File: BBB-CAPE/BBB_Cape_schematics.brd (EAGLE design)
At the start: 160 x 176.5 mm, 94 parts, among them IC1 EEPROM-I2CSMD, SW2 219-02, U5 TPS60403

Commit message: Route all components in PCB in BBB_Cape_schematics.brd
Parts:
- removed C1: 0.1uF, logic-supply:C0402
- removed C11: 0.0015uF, rcl:C1206
- removed IC1: EEPROM-I2CSMD, logic-supply:SO08
- removed R1, R2, R3, R4, R5, R6: 5.6k, logic-supply:R0402
- removed R25: 4.99k, resistor:M1206
- removed S2, SW2: 219-02, switch-dil:CTS-219-02
- removed SJ10, SJ11, SJ12, SJ13, SJ2, SJ3, SJ4, SJ5, SJ6, SJ7, SJ8, SJ9: (no value), jumper:SJW
- removed TP1, TP2: TEST_POINT, logic-supply:TEST_POINT
- removed TP1_2.5V, TP_INA_VREF: TPB2,54, testpad:B2,54
- removed U$10: CDCS502, Components:SSOP-8
- removed U$13, U$9: OPA335, Components:SOT23-5
- removed U$16, U$18: PAD, Components:RECT_PAD
- removed U$19: ADS1252, Components:SOIC-8
- removed U$23: ATS16ASM-1, Components:CRYSTAL_SMD
- added JP1, JP2: (no value), jumper:JP3Q
- added JP3: (no value), jumper:JP2
- added JP4, JP5: (no value), jumper:JP2Q
- added LH, LH_INDEX: PAD, Components:RECT_PAD
- added U10: CDCS502, Components:SSOP-8
- added U13, U9: OPA335, Components:SOT23-5
- added U19: ADS1252, Components:SOIC-8
- added U23: ATS16ASM-1, Components:CRYSTAL_SMD
- moved TP_5V 283.6 mm to (72.0, 16.6)
- moved TP5 250.2 mm to (69.0, 46.5)
- moved TP_ECG_INA 250.1 mm to (73.4, 9.44)
- moved TP2_MIN5V 243.6 mm to (94.7, 61.6)
- moved TP4 235.5 mm to (57.0, 43.5)
- moved TP3 235.4 mm to (57.0, 49.2)
- moved TP_3.3V 221.9 mm to (45.4, 71.1)
- moved TP_ECG_LPF 220.4 mm to (77.8, 39.7)
- moved TP1_MIN5V 212.6 mm to (70.3, 67.2)
- moved TP2_2.5V 46.8 mm to (56.6, 34.5)
- moved R24 15.0 mm to (68.6, 34.0), turned to 180 degrees
- moved C10 12.7 mm to (77.5, 35.1), turned to 0 degrees
- moved R18 12.1 mm to (87.0, 26.4), turned to 270 degrees
- moved R17 11.4 mm to (68.6, 29.0), turned to 180 degrees
- moved R26 11.2 mm to (68.6, 23.9), turned to 180 degrees
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- renumbered U$11 to U11, U$12 to U12, U$14 to U14, U$17 to RH, U$21 to U21, U$22 to U22, U$24 to RH_INDEX, U$4 to U4
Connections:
- removed net N$13: IC1.1, R3.1, SW2.4
- removed net N$14: IC1.2, R2.1, SW2.3
- removed net N$15: IC1.3, R1.1
- removed net N$39: R26.2, SJ7.2
- removed net N$43: C20.1, SJ13.2
- removed net WP: IC1.7, R4.1, TP2.P$1
- net +5V/2: now also U13.P$3, U19.P$2, U19.P$8, U9.P$3; no longer U$13.P$3, U$19.P$2, U$19.P$8, U$9.P$3
- net 3.3V: now also JP5.2, JP5.4, U10.7; no longer C1.1, IC1.8, R1.2, R2.2, R3.2, R4.2, R5.2, R6.2, S2.1, S2.2, U$10.7
- net 5V: now also U13.P$5, U19.P$3, U9.P$5; no longer U$13.P$5, U$19.P$3, U$9.P$5
- net ADC_DOUT: now also U19.P$5; no longer U$19.P$5
- net ADC_SCLK: now also U19.P$6; no longer U$19.P$6
- net ECG_LPF: now also U13.P$1, U19.P$1; no longer C11.2, U$13.P$1, U$19.P$1
- net GND: now also JP3.2, U10.4, U10.5, U13.P$2, U19.P$7, U9.P$2; no longer C1.2, IC1.4, SJ8.1, SW2.1, SW2.2, TP1.P$1, U$10.4, U$10.5, U$13.P$2, U$19.P$7, U$9.P$2
- net I2C2_SCL: no longer IC1.6, R5.1
- net I2C2_SDA: no longer IC1.5, R6.1
- net N$10: now also JP3.3; no longer SJ8.2, SJ9.2
- net N$11: now also JP1.2, JP1.4, JP1.6, JP4.2, JP4.4; no longer SJ2.1, SJ3.1, SJ4.1, SJ5.1, SJ6.1, SJ7.1
- net N$12: now also U9.P$4; no longer U$9.P$4
- net N$18: now also JP2.2, JP2.4, JP2.6, U13.P$4; no longer R25.1, SJ10.1, SJ11.1, SJ12.1, SJ13.1, U$13.P$4
- net N$22: now also LH_INDEX.P$1; no longer U$18.P$1
- net N$24: now also LH.P$1; no longer U$16.P$1
- net N$26: no longer TP1_2.5V.TP
- net N$27: now also U10.1, U23.P$1; no longer U$10.1, U$23.P$1
- net N$28: now also U10.8, U23.P$2; no longer U$10.8, U$23.P$2
- net N$29: now also U10.6, U19.P$4; no longer U$10.6, U$19.P$4
- net N$30: now also JP5.3, U10.2; no longer S2.4, U$10.2
- net N$31: now also JP5.1, U10.3; no longer S2.3, U$10.3
- net N$33: now also JP4.3; no longer SJ2.2
- net N$34: now also JP4.1; no longer SJ3.2
- net N$35: now also JP3.1, U9.P$1; no longer SJ9.1, TP_INA_VREF.TP, U$9.P$1
- net N$36: now also JP1.5, R24.2; no longer R25.2, SJ4.2
- net N$37: now also JP1.3, R17.2; no longer R24.2, SJ5.2
- net N$38: now also JP1.1, R26.2; no longer R17.2, SJ6.2
- net N$40: now also C10.1, JP2.5; no longer C11.1, SJ10.2
- net N$41: now also C21.1, JP2.3; no longer C10.1, SJ11.2
- net N$42: now also C20.1, JP2.1; no longer C21.1, SJ12.2
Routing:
- net 5V: track 198.7 -> 298.7 mm
- net 3.3V: track 2.54 -> 66.3 mm, vias 0 -> 1
- net ECG_LPF: track 0.00 -> 51.0 mm
- net N$18: track 0.00 -> 46.9 mm
- net N$11: track 8.62 -> 43.6 mm
- net +5V/2: track 135.9 -> 168.3 mm, vias 1 -> 4
- net N$10: track 6.04 -> 35.5 mm
- net N$12: track 10.1 -> 28.7 mm
- net N$30: track 0.00 -> 15.7 mm
- net GND: track 25.0 -> 38.9 mm, vias 9 -> 41
- net ADC_DOUT: track 0.00 -> 12.7 mm
- net ADC_SCLK: track 0.00 -> 11.7 mm
- net N$29: track 0.00 -> 10.4 mm
- net N$31: track 0.00 -> 10.4 mm
- net N$38: track 0.00 -> 6.15 mm
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- added copper zone on layer 1, net GND

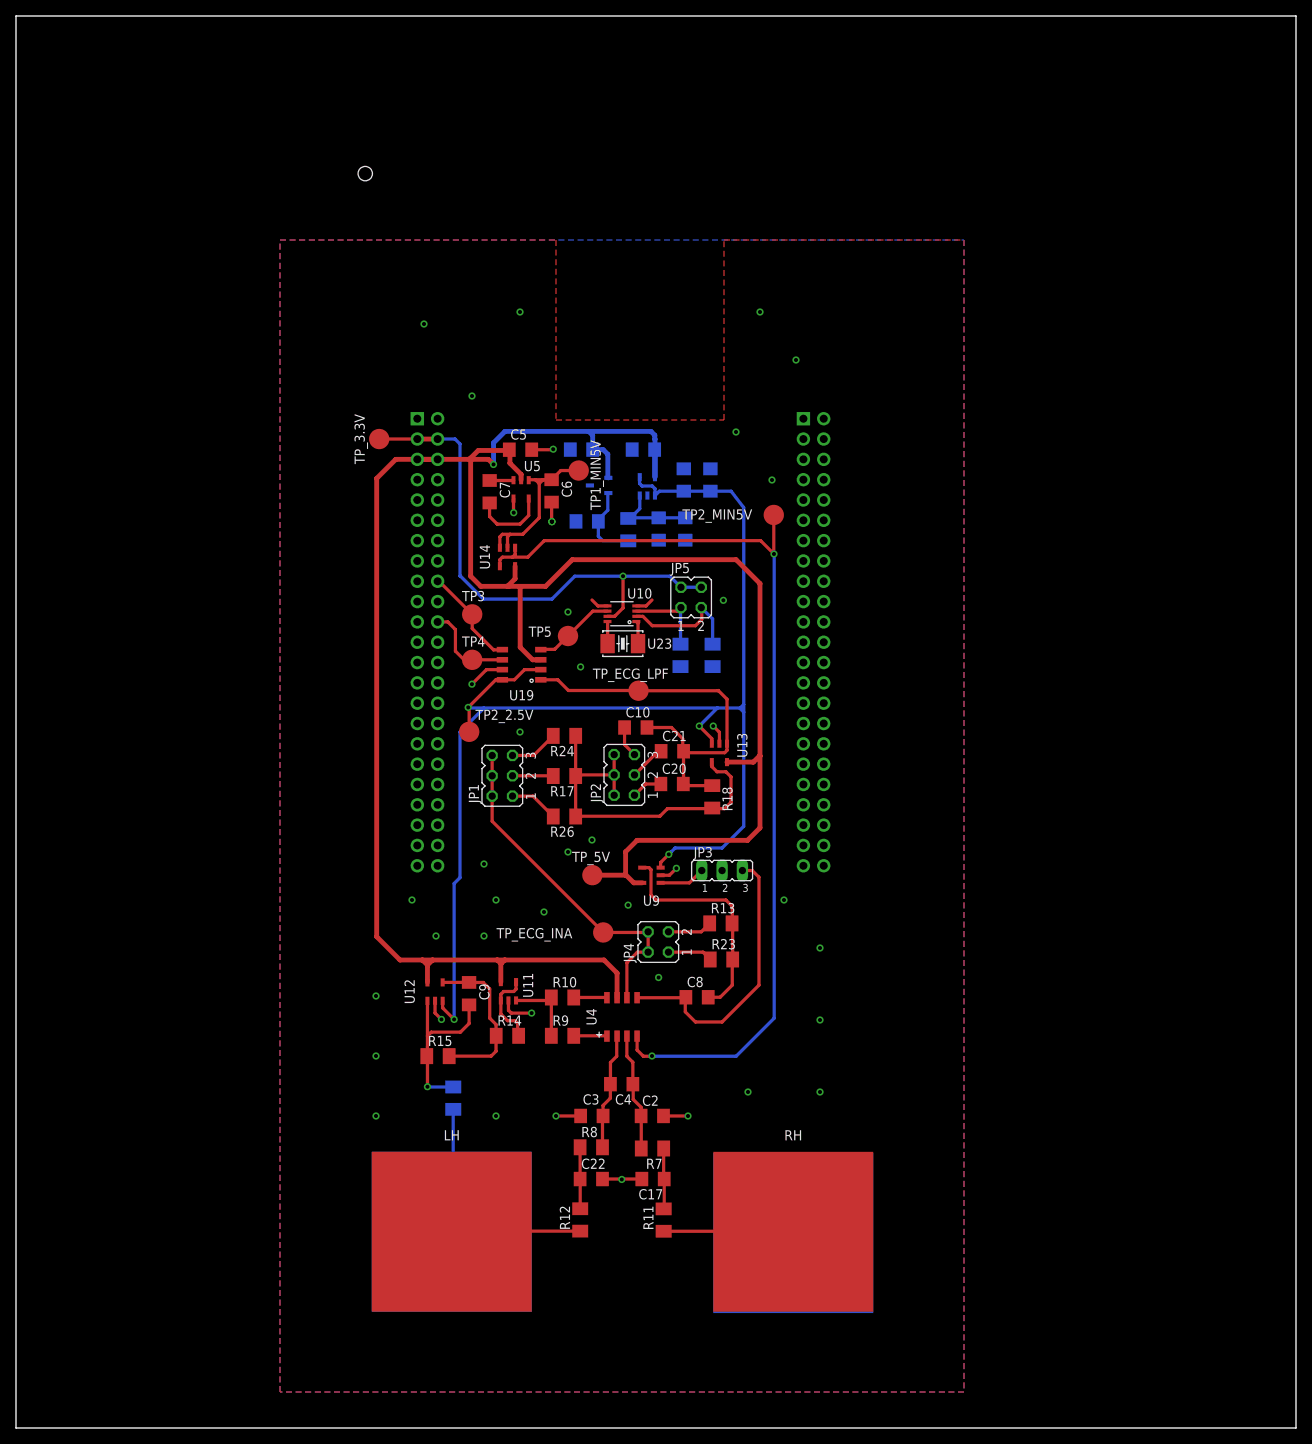
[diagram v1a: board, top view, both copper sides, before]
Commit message: Modify board boundary, Change orientation of Component names in Silk screen
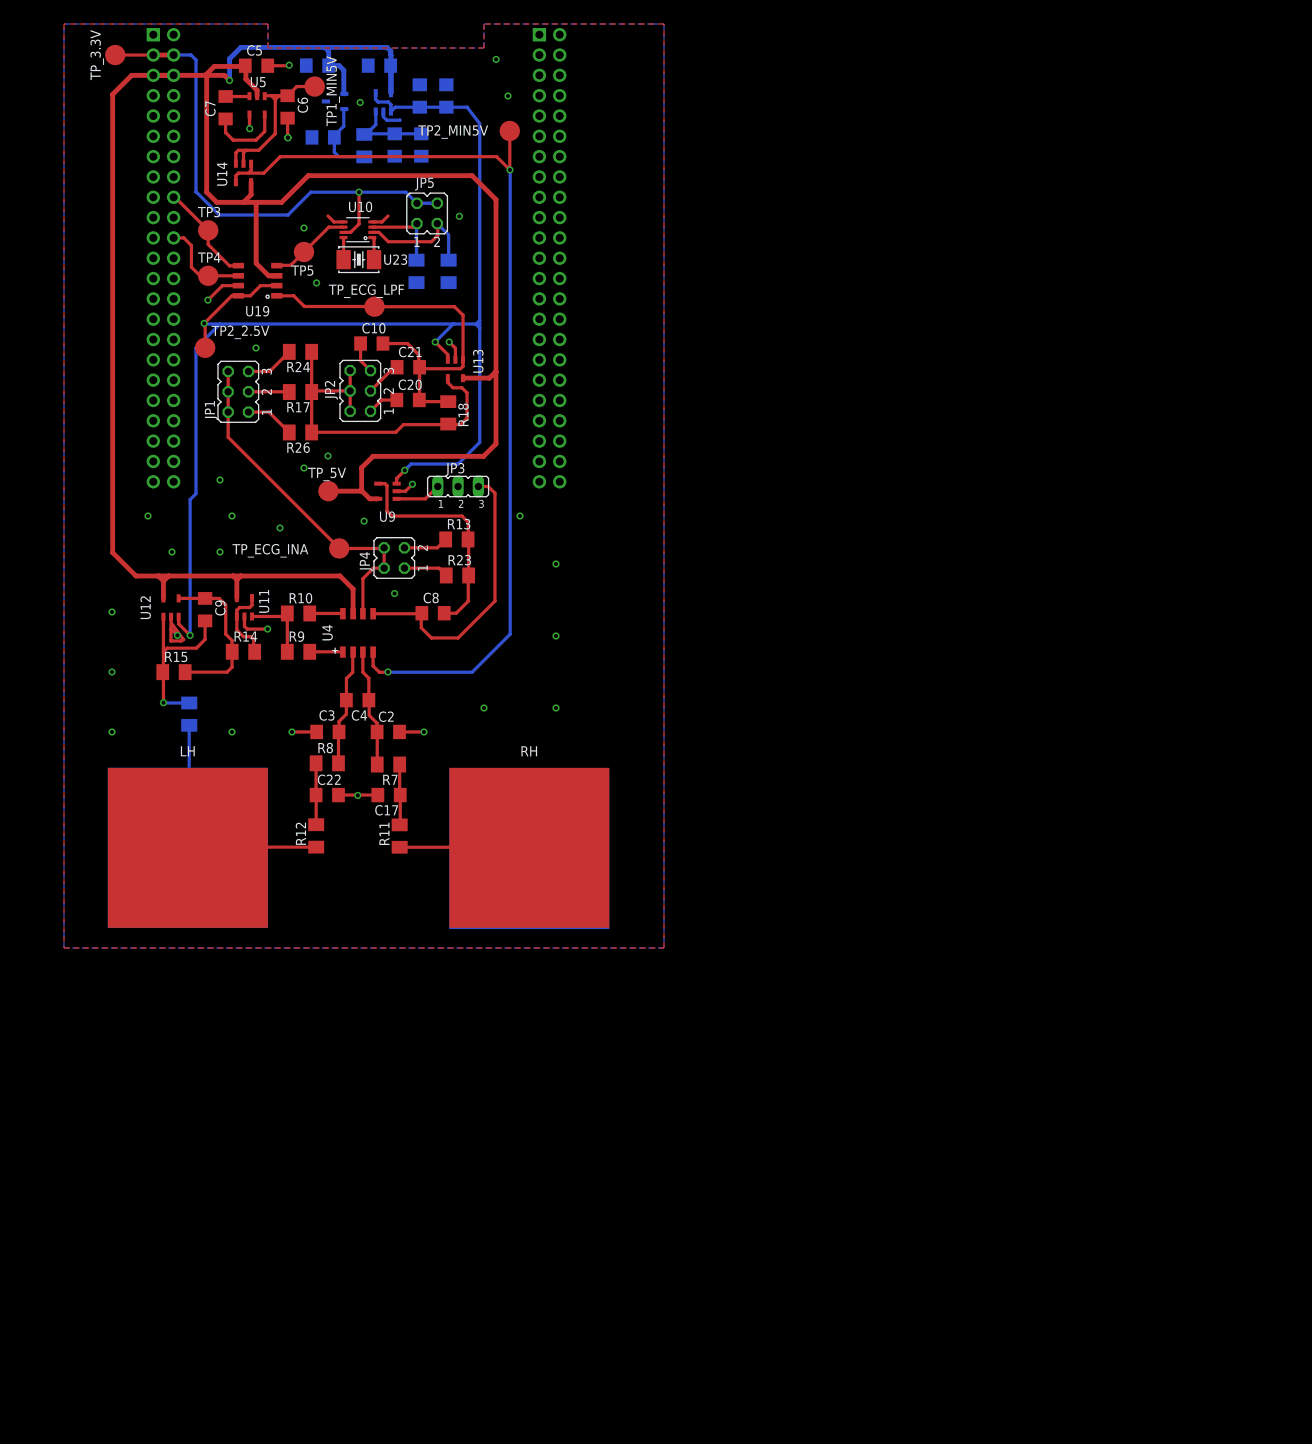
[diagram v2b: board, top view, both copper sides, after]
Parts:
- removed U$25: LCD_4D, Components:LCD_4D
- moved U23 58.2 mm to (42.9, 93.5)
- moved BB1 58.2 mm to (69.9, 140.7)
- moved C10 58.2 mm to (44.5, 83.1)
- moved C13 58.2 mm to (37.7, 117.8)
- moved C15 58.2 mm to (50.7, 107.9)
- moved C16 58.2 mm to (47.3, 107.9)
- moved C17 58.2 mm to (46.6, 26.6)
- moved C19 58.2 mm to (53.8, 114.0)
- moved C20 58.2 mm to (49.0, 76.0)
- moved C21 58.2 mm to (49.0, 80.1)
- moved C3 58.2 mm to (39.0, 34.5)
- moved C4 58.2 mm to (42.7, 38.5)
- moved C5 58.2 mm to (30.1, 117.8)
- moved C6 58.2 mm to (34.0, 112.6)
- moved C7 58.2 mm to (26.2, 112.5)
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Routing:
- net N$13: track 0.00 -> 5.50 mm
- net GND: track 38.9 -> 41.9 mm, vias 41 -> 37
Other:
- board outline removed

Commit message: Update Resistor and Capacitor value in BBB_Cape_schematics.sch
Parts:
- C20: value 0.0015uF -> 0.015uF
- C21: value 0.0015uF -> 0.0047uF
- R17: value 1.24k -> 2.49k
- R19: value 100k -> 10k
- R24: value 2.49k -> 4.99k
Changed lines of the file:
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@@
 <?xml version="1.0" encoding="utf-8"?>
 <!DOCTYPE eagle SYSTEM "eagle.dtd">
-<eagle version="6.4">
+<eagle version="6.2">
 <drawing>
 <settings>
@@
 </class>
 </classes>
-<designrules name="default">
+<designrules>
 <description language="de">&lt;b&gt;EAGLE Design Rules&lt;/b&gt;
 &lt;p&gt;
@@
 <attribute name="NAME" x="57.15" y="80.8375" size="1.27" layer="21" rot="R270" align="bottom-center"/>
 </element>
-<element name="R17" library="resistor" package="M1206" value="1.24k" x="35.55875" y="76.9975" rot="R180"/>
+<element name="R17" library="resistor" package="M1206" value="2.49k" x="35.55875" y="76.9975" rot="R180"/>
 <element name="R18" library="resistor" package="M1206" value="1M" x="54.02875" y="74.3975" smashed="yes" rot="R270">
 <attribute name="NAME" x="55.29875" y="75.6675" size="1.27" layer="25" rot="R270"/>
@@
 </element>
 <element name="C13" library="rcl" package="C1206" value="0.1uF" x="37.685" y="117.79625" rot="MR0"/>
-<element name="R19" library="resistor" package="M1206" value="100k" x="43.53625" y="107.79375" smashed="yes" rot="MR90">
+<element name="R19" library="resistor" package="M1206" value="10k" x="43.53625" y="107.79375" smashed="yes" rot="MR90">
 <attribute name="NAME" x="41.155" y="106.20625" size="1.27" layer="26" rot="MR90"/>
 <attribute name="VALUE" x="40.99625" y="106.52375" size="1.27" layer="28" rot="MR90"/>
@@
 <element name="R21" library="resistor" package="M1206" value="10k" x="54.07375" y="92.075" rot="MR90"/>
 <element name="R23" library="resistor" package="M1206" value="80.6k" x="55.18375" y="54.07"/>
-<element name="R24" library="resistor" package="M1206" value="2.49k" x="35.55875" y="82.01625" rot="R180"/>
+<element name="R24" library="resistor" package="M1206" value="4.99k" x="35.55875" y="82.01625" rot="R180"/>
 <element name="R26" library="resistor" package="M1206" value="0.825k" x="35.55875" y="71.945" rot="R180"/>
 <element name="C10" library="rcl" package="C1206" value="0.0015uF" x="44.4725" y="83.06"/>
-<element name="C20" library="rcl" package="C1206" value="0.0015uF" x="49.01125" y="75.9975"/>
-<element name="C21" library="rcl" package="C1206" value="0.0015uF" x="49.04375" y="80.0925"/>
+<element name="C20" library="rcl" package="C1206" value="0.015uF" x="49.01125" y="75.9975"/>
+<element name="C21" library="rcl" package="C1206" value="0.0047uF" x="49.04375" y="80.0925"/>
 <element name="RH_INDEX" library="Components" package="RECT_PAD" value="PAD" x="64.15875" y="19.865" rot="MR0"/>
 <element name="C12" library="rcl" package="C1206" value="0.10uF" x="45.42875" y="117.79375" rot="MR0"/>
